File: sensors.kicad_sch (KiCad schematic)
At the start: 0 parts

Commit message: Added some components
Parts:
- added U401: LPS22HH, Package_LGA:ST_HLGA-10_2x2mm_P0.5mm_LayoutBorder3x2y, symbol Sensor_Pressure:LPS22HH
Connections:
- new net: U401.8 (GND), U401.9 (GND)
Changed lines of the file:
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@@
 (kicad_sch (version 20230121) (generator eeschema)
   (paper "A4")
+  (symbol (lib_id "Sensor_Pressure:LPS22HH") (at 74.295 81.28 0) (unit 1)
+    (in_bom yes) (on_board yes) (dnp no) (fields_autoplaced)
+    (property "Reference" "U401" (at 62.23 78.74 0)
+      (effects (font (size 1.27 1.27)) (justify right))
+    )
+    (property "Value" "LPS22HH" (at 62.23 81.28 0)
+      (effects (font (size 1.27 1.27)) (justify right))
+    )
+    (property "Footprint" "Package_LGA:ST_HLGA-10_2x2mm_P0.5mm_LayoutBorder3x2y" (at 75.565 92.71 0)
+      (effects (font (size 1.27 1.27)) (justify left) hide)
+    )
+    (property "Datasheet" "https://www.st.com/resource/en/datasheet/lps22hh.pdf" (at 75.565 95.25 0)
+      (effects (font (size 1.27 1.27)) (justify left) hide)
+    )
+    (pin "1")
+    (pin "10")
+    (pin "2")
+    (pin "3")
+    (pin "4")
+    (pin "5")
+    (pin "6")
+    (pin "7")
+    (pin "8")
+    (pin "9")
+    (instances
+      (project "MicroQuad"
+        (path "/8971f876-5b3c-4165-aa17-84d4a3cd004e/9d5bdf31-14a7-425b-9f7f-c51db060d3a1"
+          (reference "U401") (unit 1)
+        )
+      )
+    )
+  )
 )

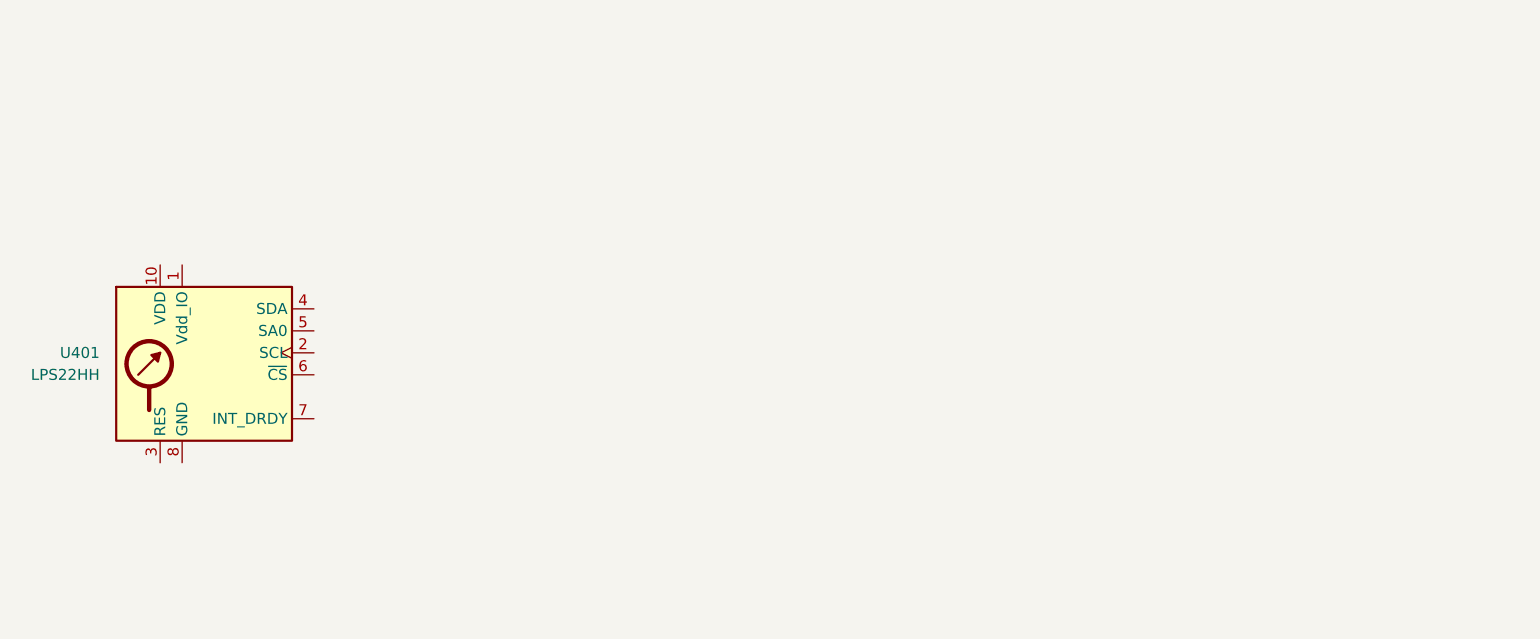
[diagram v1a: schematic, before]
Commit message: Finished cconnections for imu
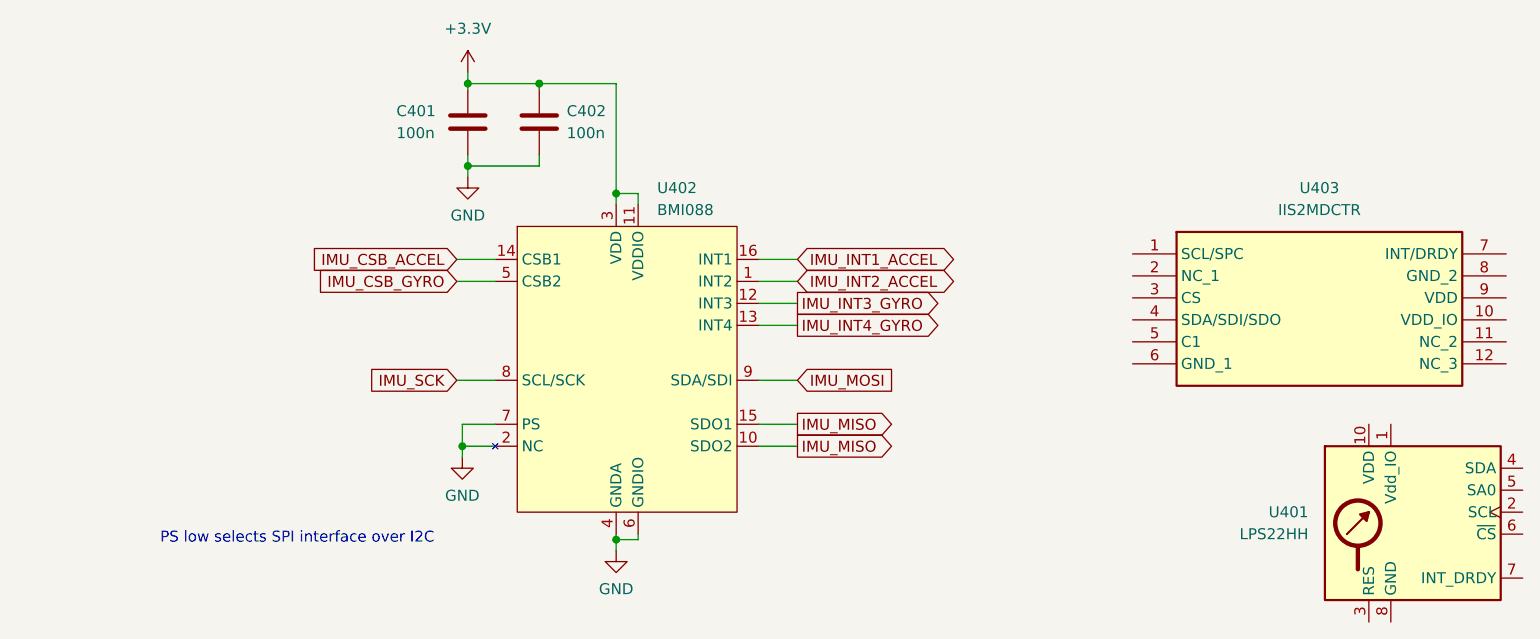
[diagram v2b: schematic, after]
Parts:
- added C401, C402: 100n, symbol Device:C
- added U402: BMI088, symbol Custom_Symbols_KiCAD7:BMI088
- added U403: IIS2MDCTR, IIS2MDCTR, symbol IIS2MDCTR:IIS2MDCTR
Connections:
- new net +3.3V: C401.1, C402.1, U402.11 (VDDIO), U402.3 (VDD)
- new net GND: C401.2, C402.2, U402.2 (NC), U402.4 (GNDA), U402.6 (GNDIO), U402.7 (PS)
- new net IMU_CSB_ACCEL: U402.14 (CSB1)
- new net IMU_CSB_GYRO: U402.5 (CSB2)
- new net IMU_INT1_ACCEL: U402.16 (INT1)
- new net IMU_INT2_ACCEL: U402.1 (INT2)
- new net IMU_INT3_GYRO: U402.12 (INT3)
- new net IMU_INT4_GYRO: U402.13 (INT4)
- new net IMU_MISO: U402.10 (SDO2), U402.15 (SDO1)
- new net IMU_MOSI: U402.9 (SDA/SDI)
- new net IMU_SCK: U402.8 (SCL/SCK)
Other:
- note added: "PS low selects SPI interface over I2C"
- moved on the sheet: U401

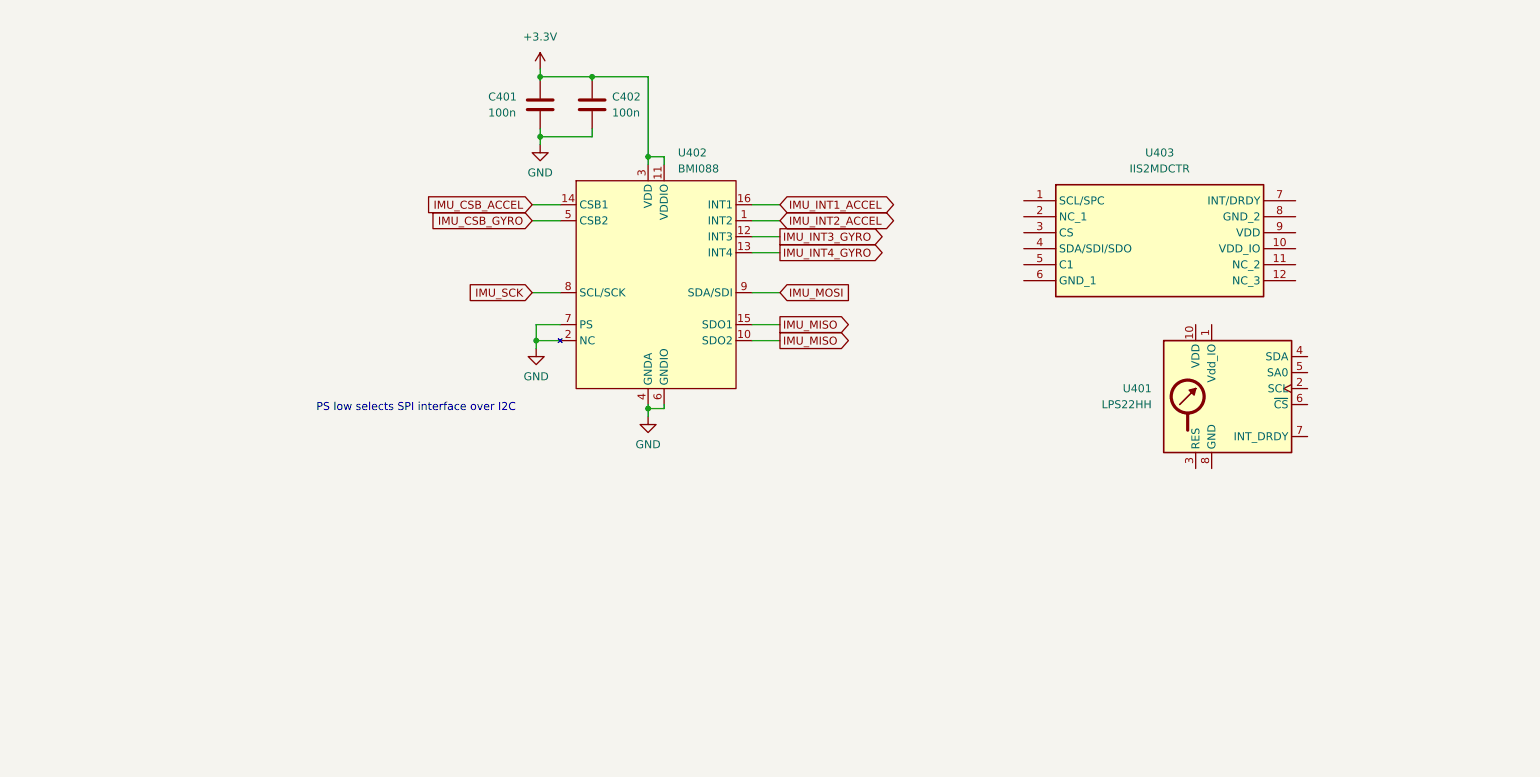
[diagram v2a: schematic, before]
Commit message: Finished wiring for barometer
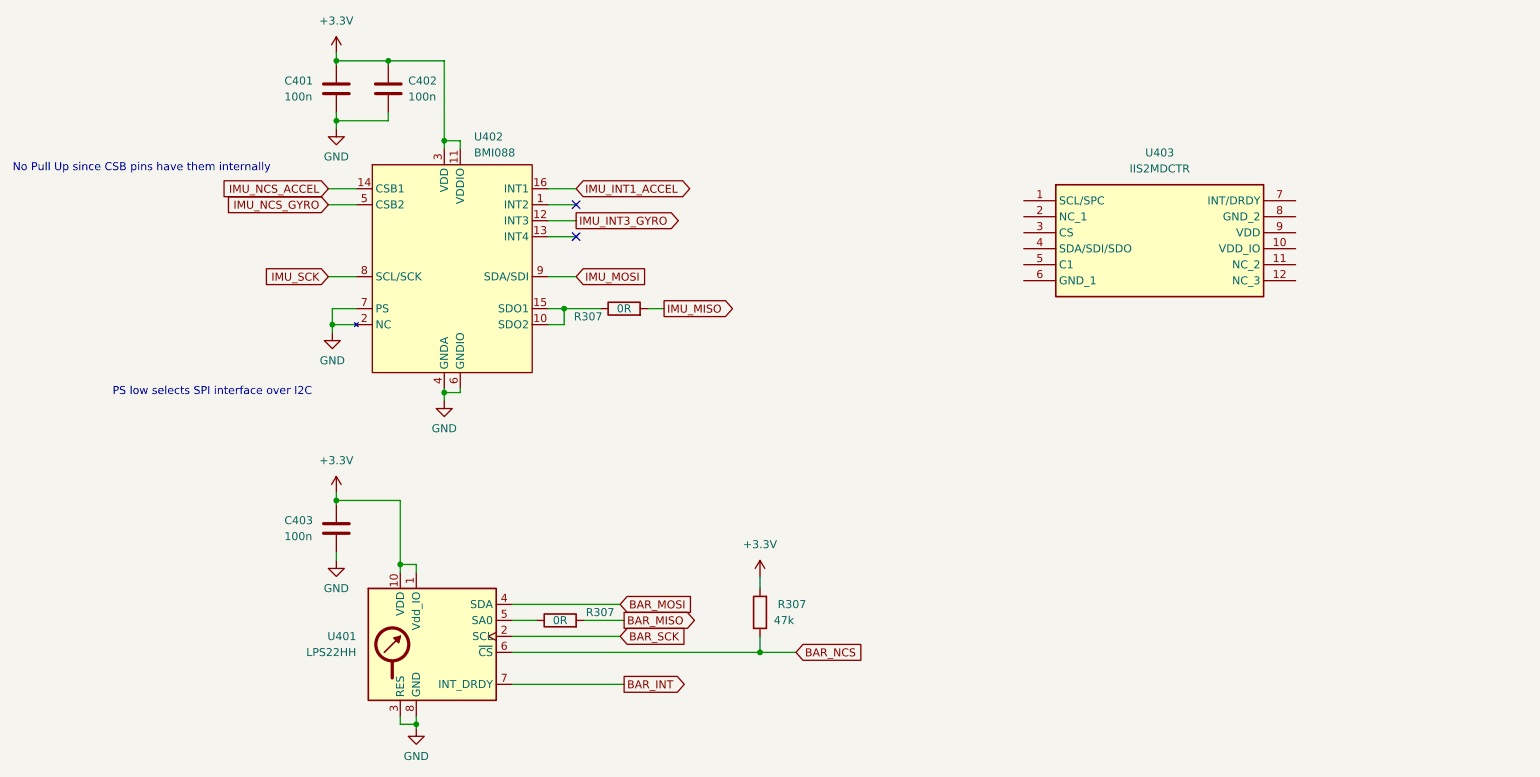
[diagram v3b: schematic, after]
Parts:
- added C403: 100n, symbol Device:C
- added R307: 47k, symbol Device:R
- added R307 (x2): 0R, symbol Device:R
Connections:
- net +3.3V: now also U401.1 (Vdd_IO), U401.10 (VDD), C403.1, R307.2
- net GND: now also U401.3 (RES), U401.8 (GND), U401.9 (GND), C403.2
- net IMU_MISO: now also R307.2; no longer U402.10 (SDO2), U402.15 (SDO1)
- net BAR_SCK: now reaches U401.2 (SCL)
- net BAR_MOSI: now reaches U401.4 (SDA)
- net at U401.5 (SA0): now also R307.1
- net BAR_NCS: now reaches U401.6 (~{CS})
- net BAR_NCS: now also R307.1
- net BAR_INT: now reaches U401.7 (INT_DRDY)
- net IMU_CSB_ACCEL renamed IMU_NCS_ACCEL
- net IMU_CSB_GYRO renamed IMU_NCS_GYRO
- net IMU_INT2_ACCEL: no longer names the net of U402.1 (INT2)
- net IMU_INT4_GYRO: no longer names the net of U402.13 (INT4)
- new net: R307.1, U402.10 (SDO2), U402.15 (SDO1)
- new net BAR_MISO: R307.2
- no-connect marks 0 -> 2
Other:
- note added: "No Pull Up since CSB pins have them internally"
- moved on the sheet: C401, C402, U401, U402

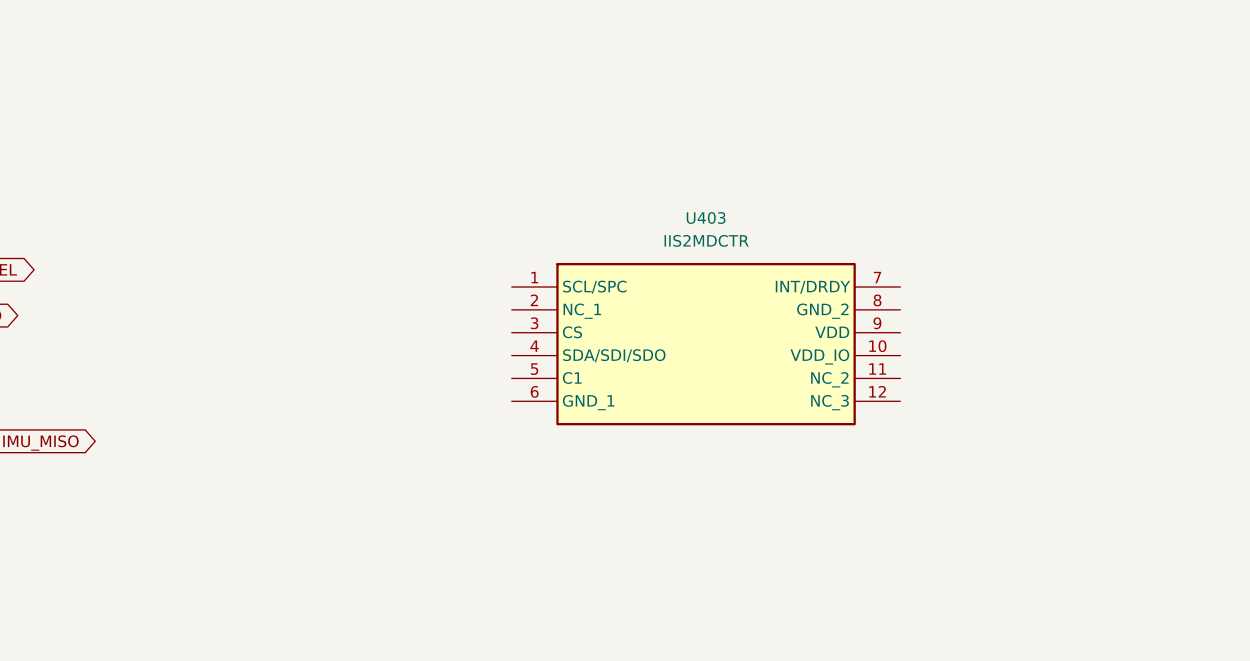
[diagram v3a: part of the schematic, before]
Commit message: Added magnetometer circuitry
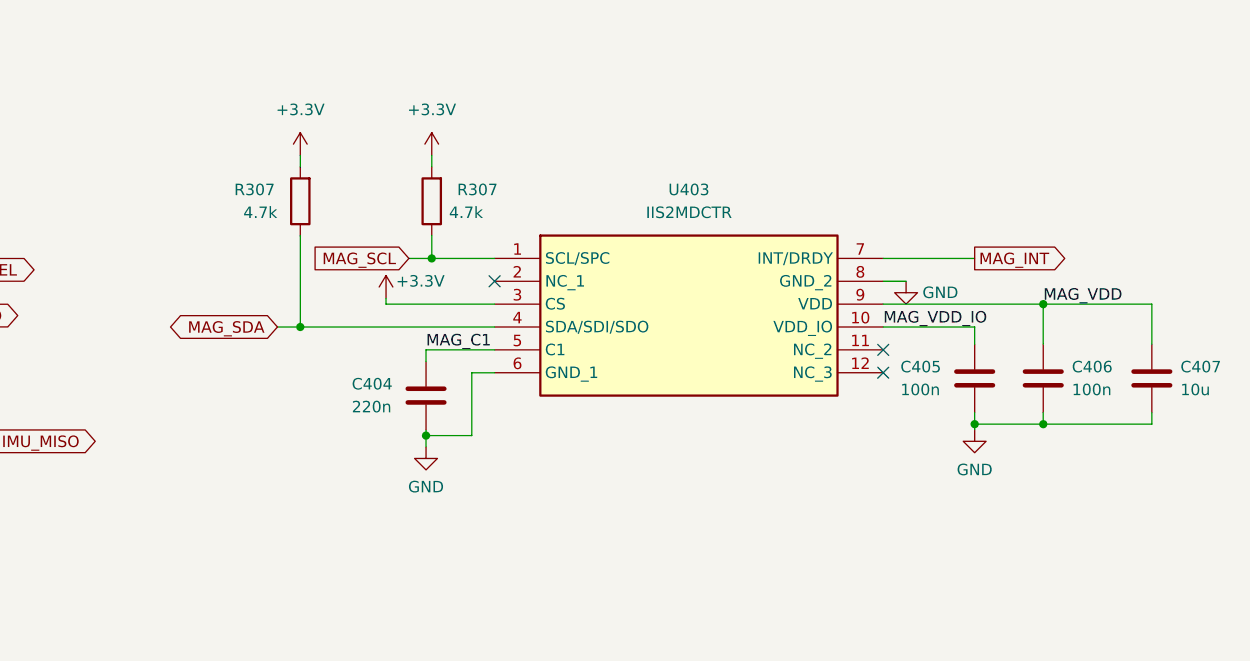
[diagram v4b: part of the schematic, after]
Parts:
- added C404: 220n, symbol Device:C
- added C405, C406: 100n, symbol Device:C
- added C407: 10u, symbol Device:C
- added R307 (x2): 4.7k, symbol Device:R
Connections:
- net +3.3V: now also U403.3 (CS), R307.2, R307.2
- net GND: now also U403.6 (GND_1), U403.8 (GND_2), C404.2, C405.2, C406.2, C407.2
- net MAG_SCL: now reaches U403.1 (SCL/SPC)
- net MAG_SCL: now also R307.1
- net MAG_VDD_IO: now reaches U403.10 (VDD_IO)
- net MAG_VDD_IO: now also C405.1
- net MAG_SDA: now reaches U403.4 (SDA/SDI/SDO)
- net MAG_SDA: now also R307.1
- net MAG_C1: now reaches U403.5 (C1)
- net MAG_C1: now also C404.1
- net MAG_INT: now reaches U403.7 (INT/DRDY)
- net MAG_VDD: now reaches U403.9 (VDD)
- net MAG_VDD: now also C406.1, C407.1
- no-connect marks 2 -> 5
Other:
- moved on the sheet: U403
